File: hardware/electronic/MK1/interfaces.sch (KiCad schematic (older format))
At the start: 10 parts, among them P1 CONN_01X08, P2 CONN_01X06, P3 CONN_01X10, P4 CONN_01X08, U6 RN4871

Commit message: HW: Minor cleanup in the schematics and layout
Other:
- note added: "Radio"
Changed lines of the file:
@@
 Text HLabel 3900 1500 2    60   Input ~ 0
 3V3
+Text Notes 6700 950  0    157  ~ 0
+Radio
 $EndSCHEMATC

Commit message: HW: Add missing component values
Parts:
- P1, P4: value CONN_01X08 -> 3M 939850-01-08-RA
- P2: value CONN_01X06 -> 3M 929870-01-06-RA
- P3: value CONN_01X10 -> 3M 929870-01-10-RA
- Radio_UART_Debug1: value Radio_UART -> MOLEX 22-28-4054
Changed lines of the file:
@@
 P 3700 1750
 F 0 "P3" H 3700 2300 50  0000 C CNN
-F 1 "CONN_01X10" V 3800 1750 50  0000 C CNN
+F 1 "3M 929870-01-10-RA" V 3800 1750 50  0000 C CNN
 F 2 "Socket_Strips:Socket_Strip_Straight_1x10" H 3700 1750 50  0001 C CNN
 F 3 "" H 3700 1750 50  0000 C CNN
@@
 P 3700 2800
 F 0 "P4" H 3700 3250 50  0000 C CNN
-F 1 "CONN_01X08" V 3800 2800 50  0000 C CNN
+F 1 "3M 939850-01-08-RA" V 3800 2800 50  0000 C CNN
 F 2 "Socket_Strips:Socket_Strip_Straight_1x08" H 3700 2800 50  0001 C CNN
 F 3 "" H 3700 2800 50  0000 C CNN
@@
 P 2100 2050
 F 0 "P1" H 2100 2500 50  0000 C CNN
-F 1 "CONN_01X08" V 2200 2050 50  0000 C CNN
+F 1 "3M 939850-01-08-RA" V 2200 2050 50  0000 C CNN
 F 2 "Socket_Strips:Socket_Strip_Straight_1x08" H 2100 2050 50  0001 C CNN
 F 3 "" H 2100 2050 50  0000 C CNN
@@
 P 2100 2900
 F 0 "P2" H 2100 3250 50  0000 C CNN
-F 1 "CONN_01X06" V 2200 2900 50  0000 C CNN
+F 1 "3M 929870-01-06-RA" V 2200 2900 50  0000 C CNN
 F 2 "Socket_Strips:Socket_Strip_Straight_1x06" H 2100 2900 50  0001 C CNN
 F 3 "" H 2100 2900 50  0000 C CNN
@@
 P 6300 3150
 F 0 "Radio_UART_Debug1" V 6400 3150 50  0000 C CNN
-F 1 "Radio_UART" V 6400 3150 50  0001 C CNN
+F 1 "MOLEX 22-28-4054" V 6400 3150 50  0001 C CNN
 F 2 "Pin_Headers:Pin_Header_Straight_1x05" H 6300 3150 50  0001 C CNN
 F 3 "" H 6300 3150 50  0000 C CNN

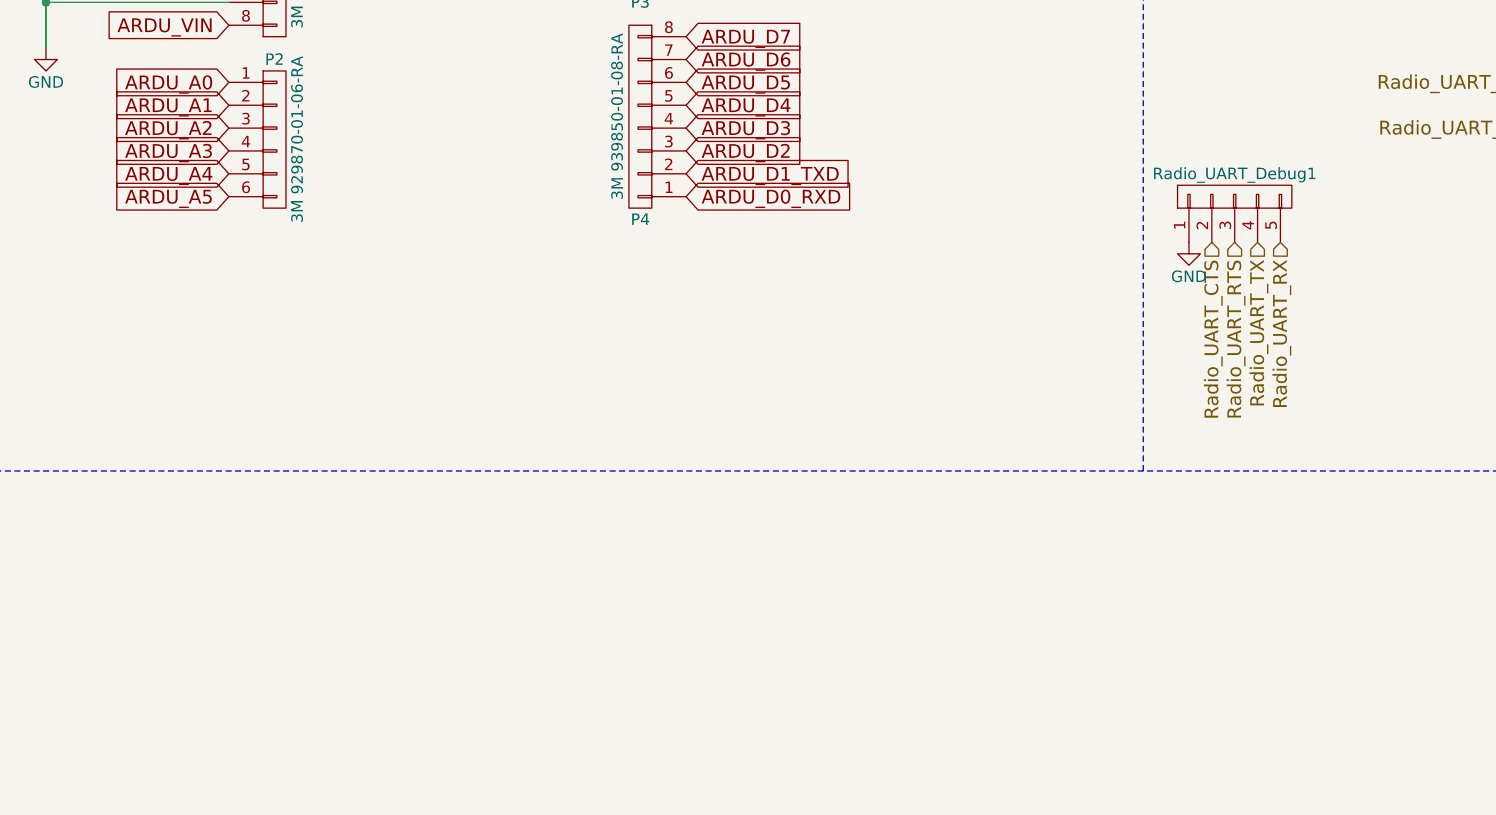
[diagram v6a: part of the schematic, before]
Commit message: HW: Add 6 mounting holes in the center of the frame
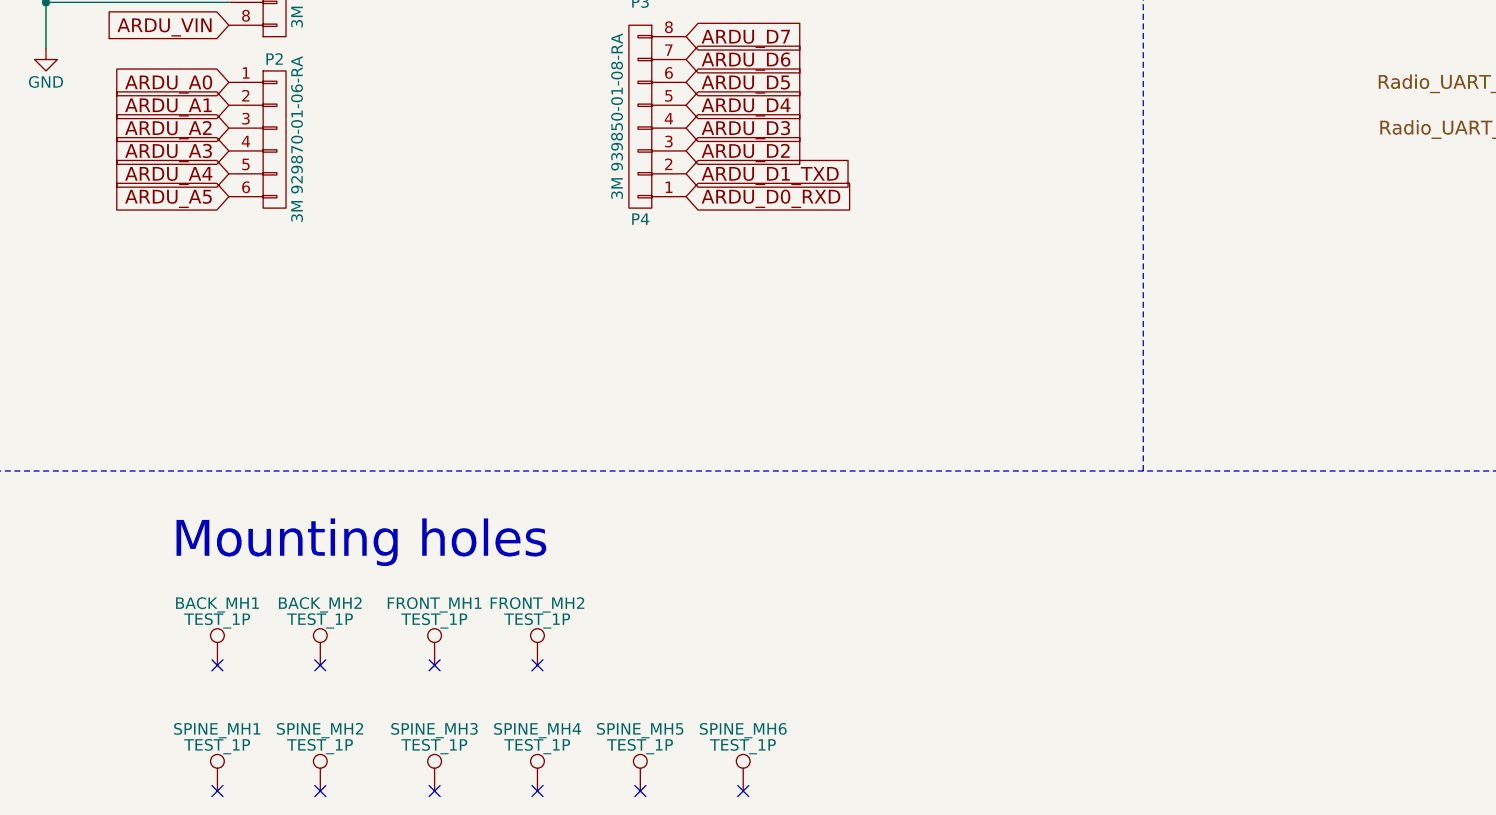
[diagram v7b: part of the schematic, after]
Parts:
- removed Radio_UART_Debug1: MOLEX 22-28-4054, Pin_Headers:Pin_Header_Straight_1x05, symbol CONN_01X05
- added BACK_MH1, BACK_MH2, FRONT_MH1, FRONT_MH2, SPINE_MH1, SPINE_MH2, SPINE_MH3, SPINE_MH4, SPINE_MH5, SPINE_MH6: TEST_1P, Mounting_Holes:MountingHole_3.2mm_M3_Pad, symbol TEST_1P
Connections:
- no-connect marks 8 -> 18
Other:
- note added: "Mounting holes"
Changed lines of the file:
@@
 ARDU_A5
 $Comp
-L GND #PWR020
+L GND #PWR20
 U 1 1 5886770A
 P 1100 2500
-F 0 "#PWR020" H 1100 2250 50  0001 C CNN
+F 0 "#PWR20" H 1100 2250 50  0001 C CNN
 F 1 "GND" H 1100 2350 50  0000 C CNN
 F 2 "" H 1100 2500 50  0000 C CNN
@@
 NoConn ~ 1900 1700
 $Comp
-L GND #PWR021
+L GND #PWR21
 U 1 1 5886A835
 P 5000 1900
-F 0 "#PWR021" H 5000 1650 50  0001 C CNN
+F 0 "#PWR21" H 5000 1650 50  0001 C CNN
 F 1 "GND" H 5000 1750 50  0000 C CNN
 F 2 "" H 5000 1900 50  0000 C CNN
@@
 Radio_VCC
 $Comp
-L GND #PWR022
+L GND #PWR23
 U 1 1 5890972B
 P 8400 4000
-F 0 "#PWR022" H 8400 3750 50  0001 C CNN
+F 0 "#PWR23" H 8400 3750 50  0001 C CNN
 F 1 "GND" H 8400 3850 50  0000 C CNN
 F 2 "" H 8400 4000 50  0000 C CNN
@@
 	8400 1250 8400 1650
 $Comp
-L GND #PWR023
+L GND #PWR24
 U 1 1 58909C4C
 P 9500 1700
-F 0 "#PWR023" H 9500 1450 50  0001 C CNN
+F 0 "#PWR24" H 9500 1450 50  0001 C CNN
 F 1 "GND" H 9500 1550 50  0000 C CNN
 F 2 "" H 9500 1700 50  0000 C CNN
@@
 	9500 1500 9500 1400
 Connection ~ 9500 1400
-Text HLabel 6300 3350 3    60   Input ~ 0
-Radio_UART_RTS
-Text HLabel 6200 3350 3    60   Input ~ 0
-Radio_UART_CTS
-Text HLabel 6500 3350 3    60   Input ~ 0
-Radio_UART_RX
-Text HLabel 6400 3350 3    60   Input ~ 0
-Radio_UART_TX
-$Comp
-L CONN_01X05 Radio_UART_Debug1
-U 1 1 58936C45
-P 6300 3150
-F 0 "Radio_UART_Debug1" V 6400 3150 50  0000 C CNN
-F 1 "MOLEX 22-28-4054" V 6400 3150 50  0001 C CNN
-F 2 "Pin_Headers:Pin_Header_Straight_1x05" H 6300 3150 50  0001 C CNN
-F 3 "" H 6300 3150 50  0000 C CNN
-	1    6300 3150
-	0    -1   -1   0
-$EndComp
-$Comp
-L GND #PWR024
-U 1 1 58936DB2
-P 6100 3350
-F 0 "#PWR024" H 6100 3100 50  0001 C CNN
-F 1 "GND" H 6100 3200 50  0000 C CNN
-F 2 "" H 6100 3350 50  0000 C CNN
-F 3 "" H 6100 3350 50  0000 C CNN
-	1    6100 3350
-	1    0    0    -1
-$EndComp
 Text HLabel 3900 1500 2    60   Input ~ 0
 3V3
 Text Notes 6700 950  0    157  ~ 0
 Radio
+Text Notes 1650 4750 0    157  ~ 0
+Mounting holes
+$Comp
+L TEST_1P FRONT_MH1
+U 1 1 591E2D3F
+P 2800 5200
+F 0 "FRONT_MH1" H 2800 5470 50  0000 C CNN
+F 1 "TEST_1P" H 2800 5400 50  0000 C CNN
+F 2 "Mounting_Holes:MountingHole_3.2mm_M3_Pad" H 3000 5200 50  0001 C CNN
+F 3 "" H 3000 5200 50  0000 C CNN
+	1    2800 5200
+	1    0    0    -1
+$EndComp
+NoConn ~ 2800 5200
+$Comp
+L TEST_1P FRONT_MH2
+U 1 1 591E2D47
+P 3250 5200
+F 0 "FRONT_MH2" H 3250 5470 50  0000 C CNN
+F 1 "TEST_1P" H 3250 5400 50  0000 C CNN
+F 2 "Mounting_Holes:MountingHole_3.2mm_M3_Pad" H 3450 5200 50  0001 C CNN
+F 3 "" H 3450 5200 50  0000 C CNN
+	1    3250 5200
+	1    0    0    -1
+$EndComp
+NoConn ~ 3250 5200
+$Comp
+L TEST_1P BACK_MH1
+U 1 1 591E2D4F
+P 1850 5200
+F 0 "BACK_MH1" H 1850 5470 50  0000 C CNN
+F 1 "TEST_1P" H 1850 5400 50  0000 C CNN
+F 2 "Mounting_Holes:MountingHole_3.2mm_M3_Pad" H 2050 5200 50  0001 C CNN
+F 3 "" H 2050 5200 50  0000 C CNN
+	1    1850 5200
+	1    0    0    -1
+$EndComp
+NoConn ~ 1850 5200
+$Comp
+L TEST_1P BACK_MH2
+U 1 1 591E2D57
+P 2300 5200
+F 0 "BACK_MH2" H 2300 5470 50  0000 C CNN
+F 1 "TEST_1P" H 2300 5400 50  0000 C CNN
+F 2 "Mounting_Holes:MountingHole_3.2mm_M3_Pad" H 2500 5200 50  0001 C CNN
+F 3 "" H 2500 5200 50  0000 C CNN
+	1    2300 5200
+	1    0    0    -1
+$EndComp
+NoConn ~ 2300 5200
+$Comp
+L TEST_1P SPINE_MH1
+U 1 1 591E2D5F
+P 1850 5750
+F 0 "SPINE_MH1" H 1850 6020 50  0000 C CNN
+F 1 "TEST_1P" H 1850 5950 50  0000 C CNN
+F 2 "Mounting_Holes:MountingHole_3.2mm_M3_Pad" H 2050 5750 50  0001 C CNN
+F 3 "" H 2050 5750 50  0000 C CNN
+	1    1850 5750
+	1    0    0    -1
+$EndComp
+$Comp
+L TEST_1P SPINE_MH2
+U 1 1 591E2D66
+P 2300 5750
+F 0 "SPINE_MH2" H 2300 6020 50  0000 C CNN
+F 1 "TEST_1P" H 2300 5950 50  0000 C CNN
+F 2 "Mounting_Holes:MountingHole_3.2mm_M3_Pad" H 2500 5750 50  0001 C CNN
+F 3 "" H 2500 5750 50  0000 C CNN
+	1    2300 5750
+	1    0    0    -1
+$EndComp
+$Comp
+L TEST_1P SPINE_MH3
+U 1 1 591E2D6D
+P 2800 5750
+F 0 "SPINE_MH3" H 2800 6020 50  0000 C CNN
+F 1 "TEST_1P" H 2800 5950 50  0000 C CNN
+F 2 "Mounting_Holes:MountingHole_3.2mm_M3_Pad" H 3000 5750 50  0001 C CNN
+F 3 "" H 3000 5750 50  0000 C CNN
+	1    2800 5750
+	1    0    0    -1
+$EndComp
+$Comp
+L TEST_1P SPINE_MH4
+U 1 1 591E2D74
+P 3250 5750
+F 0 "SPINE_MH4" H 3250 6020 50  0000 C CNN
+F 1 "TEST_1P" H 3250 5950 50  0000 C CNN
+F 2 "Mounting_Holes:MountingHole_3.2mm_M3_Pad" H 3450 5750 50  0001 C CNN
+F 3 "" H 3450 5750 50  0000 C CNN
+	1    3250 5750
+	1    0    0    -1
+$EndComp
+NoConn ~ 3250 5750
+NoConn ~ 2800 5750
+NoConn ~ 2300 5750
+NoConn ~ 1850 5750
+$Comp
+L TEST_1P SPINE_MH5
+U 1 1 591E38E8
+P 3700 5750
+F 0 "SPINE_MH5" H 3700 6020 50  0000 C CNN
+F 1 "TEST_1P" H 3700 5950 50  0000 C CNN
+F 2 "Mounting_Holes:MountingHole_3.2mm_M3_Pad" H 3900 5750 50  0001 C CNN
+F 3 "" H 3900 5750 50  0000 C CNN
+	1    3700 5750
+	1    0    0    -1
+$EndComp
+$Comp
+L TEST_1P SPINE_MH6
+U 1 1 591E3943
+P 4150 5750
+F 0 "SPINE_MH6" H 4150 6020 50  0000 C CNN
+F 1 "TEST_1P" H 4150 5950 50  0000 C CNN
+F 2 "Mounting_Holes:MountingHole_3.2mm_M3_Pad" H 4350 5750 50  0001 C CNN
+F 3 "" H 4350 5750 50  0000 C CNN
+	1    4150 5750
+	1    0    0    -1
+$EndComp
+NoConn ~ 3700 5750
+NoConn ~ 4150 5750
 $EndSCHEMATC
